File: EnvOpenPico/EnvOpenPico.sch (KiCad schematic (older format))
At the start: 55 parts, among them J2 SKRKAEE020, J3 2.54mm header 01x20, J4 2.54mm header 01x20, J5 Conn_01x03_Male, U1 TLV75533PDBVR, U3 RP2040, Y1 3225_4P

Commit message: some small adjustments
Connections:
- no-connect marks 5 -> 2
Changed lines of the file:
@@
 Wire Wire Line
 	14550 7600 14650 7600
-NoConn ~ 9050 6700
-NoConn ~ 9050 6800
-NoConn ~ 9050 7400
 NoConn ~ 1100 2000
 NoConn ~ 1100 1400

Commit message: added some notes and also various tweaks n what not.
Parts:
- FLASH1: value W25Q16 -> W25Q16FWUXIE
- RSW1: value Jumper_NO_Small -> SKRKAEE020
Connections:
- wire segments 219 -> 222
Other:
- note added: "JLCPCB Often has W25Q16FWUXIE in stock"
- note added: "Only fit cBP1 if you have selected an \nalternate voltage regulator\n\nTLV75533PDBVR does not require cBP1."
- note added: "not 22pf but pick to match crystal."
- note removed: "Only fit cBP1 if you have selected an \nalternate voltage regulator\n\nTLV75533PDBVR does not."
- moved on the sheet: PWRLED1, R12
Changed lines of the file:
@@
 P 3100 5250
 F 0 "FLASH1" H 3100 5250 50  0000 C CNN
-F 1 "W25Q16" H 3100 4750 50  0000 C CNN
+F 1 "W25Q16FWUXIE" H 3100 4750 50  0000 C CNN
 F 2 "Package_SON:SON-8-1EP_3x2mm_P0.5mm_EP1.4x1.6mm" H 3100 5250 50  0001 L BNN
 F 3 "" H 3100 5250 50  0001 L BNN
@@
 Wire Wire Line
 	3200 8400 3950 8400
-Text GLabel 6550 5800 0    50   Input ~ 0
+Text GLabel 6500 5800 0    50   Input ~ 0
 XIN
-Text GLabel 6550 6000 0    50   Input ~ 0
+Text GLabel 6500 6000 0    50   Input ~ 0
 XOUT
 Text GLabel 3950 8900 2    50   Input ~ 0
@@
 	4700 1850 4650 1850
 Text Notes 4450 2700 0    50   Italic 0
-Only fit cBP1 if you have selected an \nalternate voltage regulator\n\nTLV75533PDBVR does not.
+Only fit cBP1 if you have selected an \nalternate voltage regulator\n\nTLV75533PDBVR does not require cBP1.
 Text Notes 2200 6250 0    50   ~ 0
 GD25Q40CEIGR is NOT Compatible\nyou need GD25W16* needs to be a multiple of 8 atleast for circuitpython.
@@
 P 5800 6500
 F 0 "RSW1" H 5800 6600 50  0000 C CNN
-F 1 "Jumper_NO_Small" H 5950 6450 50  0000 C CNN
+F 1 "SKRKAEE020" H 5900 6400 50  0000 C CNN
 F 2 "Button_Switch_SMD:SW_Push_SPST_NO_Alps_SKRK" H 5800 6500 50  0001 C CNN
 F 3 "~" H 5800 6500 50  0001 C CNN
@@
 L Device:R R12
 U 1 1 614BB2FC
-P 14400 8000
-F 0 "R12" V 14193 8000 50  0000 C CNN
-F 1 "5.1K 0402 Resistor" V 14284 8000 50  0000 C CNN
-F 2 "Resistor_SMD:R_0402_1005Metric" V 14330 8000 50  0001 C CNN
-F 3 "" H 14400 8000 50  0001 C CNN
-F 4 " " H 14400 8000 50  0001 C CNN "LCSC"
-	1    14400 8000
+P 3100 2900
+F 0 "R12" V 2893 2900 50  0000 C CNN
+F 1 "5.1K 0402 Resistor" V 2984 2900 50  0000 C CNN
+F 2 "Resistor_SMD:R_0402_1005Metric" V 3030 2900 50  0001 C CNN
+F 3 "" H 3100 2900 50  0001 C CNN
+F 4 " " H 3100 2900 50  0001 C CNN "LCSC"
+	1    3100 2900
 	0    1    1    0
 $EndComp
@@
 L Device:LED PWRLED1
 U 1 1 614BBA4D
-P 14800 8000
-F 0 "PWRLED1" H 14750 7750 50  0000 C CNN
-F 1 "LED_0603" H 14600 7850 50  0000 C CNN
-F 2 "LED_SMD:LED_0603_1608Metric" H 14800 8000 50  0001 C CNN
-F 3 "" H 14800 8000 50  0001 C CNN
-F 4 " " H 14800 8000 50  0001 C CNN "LCSC"
-	1    14800 8000
+P 3500 2900
+F 0 "PWRLED1" H 3450 2650 50  0000 C CNN
+F 1 "LED_0603" H 3300 2750 50  0000 C CNN
+F 2 "LED_SMD:LED_0603_1608Metric" H 3500 2900 50  0001 C CNN
+F 3 "" H 3500 2900 50  0001 C CNN
+F 4 " " H 3500 2900 50  0001 C CNN "LCSC"
+	1    3500 2900
 	-1   0    0    1
 $EndComp
@@
 L power:GND #PWR0116
 U 1 1 614BBA57
-P 14950 8000
-F 0 "#PWR0116" H 14950 7750 50  0001 C CNN
-F 1 "GND" V 14955 7872 50  0000 R CNN
-F 2 "" H 14950 8000 50  0001 C CNN
-F 3 "" H 14950 8000 50  0001 C CNN
-	1    14950 8000
+P 3650 2900
+F 0 "#PWR0116" H 3650 2650 50  0001 C CNN
+F 1 "GND" V 3655 2772 50  0000 R CNN
+F 2 "" H 3650 2900 50  0001 C CNN
+F 3 "" H 3650 2900 50  0001 C CNN
+	1    3650 2900
 	0    -1   -1   0
 $EndComp
 Wire Wire Line
-	14550 8000 14650 8000
-Text Label 13850 8000 0    50   ~ 0
+	3250 2900 3350 2900
+Text Label 2550 2900 0    50   ~ 0
 VBUS
 Wire Wire Line
-	13850 8000 14250 8000
+	2550 2900 2950 2900
 Wire Wire Line
 	14250 7600 13850 7600
@@
 	11750 2900 11750 2850
 Connection ~ 11750 2850
+Wire Wire Line
+	3700 5550 3700 5350
+Connection ~ 3700 5550
+Text Notes 2200 6350 0    50   ~ 0
+JLCPCB Often has W25Q16FWUXIE in stock
+Text Notes 2850 8250 0    50   ~ 0
+not 22pf but pick to match crystal.
+Wire Wire Line
+	6500 5800 6550 5800
+Wire Wire Line
+	6550 6000 6500 6000
 $EndSCHEMATC

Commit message: corrected library symbol for reset button
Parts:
- RSW1: symbol Device:Jumper_NO_Small -> Switch:SW_Push
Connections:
- wire segments 222 -> 221
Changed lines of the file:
@@
 L power:GND #PWR0106
 U 1 1 6133A1A8
-P 5550 6550
-F 0 "#PWR0106" H 5550 6300 50  0001 C CNN
-F 1 "GND" H 5555 6377 50  0000 C CNN
-F 2 "" H 5550 6550 50  0001 C CNN
-F 3 "" H 5550 6550 50  0001 C CNN
-	1    5550 6550
+P 5400 6500
+F 0 "#PWR0106" H 5400 6250 50  0001 C CNN
+F 1 "GND" H 5405 6327 50  0000 C CNN
+F 2 "" H 5400 6500 50  0001 C CNN
+F 3 "" H 5400 6500 50  0001 C CNN
+	1    5400 6500
 	1    0    0    -1
 $EndComp
-Wire Wire Line
-	5550 6500 5550 6550
 $Comp
 L Regulator_Linear:AP131-15 U1
@@
 $EndComp
 $Comp
-L Device:Jumper_NO_Small RSW1
+L Switch:SW_Push RSW1
 U 1 1 6142C001
-P 5800 6500
-F 0 "RSW1" H 5800 6600 50  0000 C CNN
-F 1 "SKRKAEE020" H 5900 6400 50  0000 C CNN
-F 2 "Button_Switch_SMD:SW_Push_SPST_NO_Alps_SKRK" H 5800 6500 50  0001 C CNN
-F 3 "~" H 5800 6500 50  0001 C CNN
-	1    5800 6500
+P 5700 6500
+F 0 "RSW1" H 5700 6300 50  0000 C CNN
+F 1 "SKRKAEE020" H 5750 6400 50  0000 C CNN
+F 2 "Button_Switch_SMD:SW_Push_SPST_NO_Alps_SKRK" H 5700 6500 50  0001 C CNN
+F 3 "~" H 5700 6500 50  0001 C CNN
+	1    5700 6500
 	1    0    0    -1
 $EndComp
-Wire Wire Line
-	5550 6500 5700 6500
 Wire Wire Line
 	5900 6500 6550 6500
@@
 Wire Wire Line
 	6550 6000 6500 6000
+Wire Wire Line
+	5500 6500 5400 6500
 $EndSCHEMATC

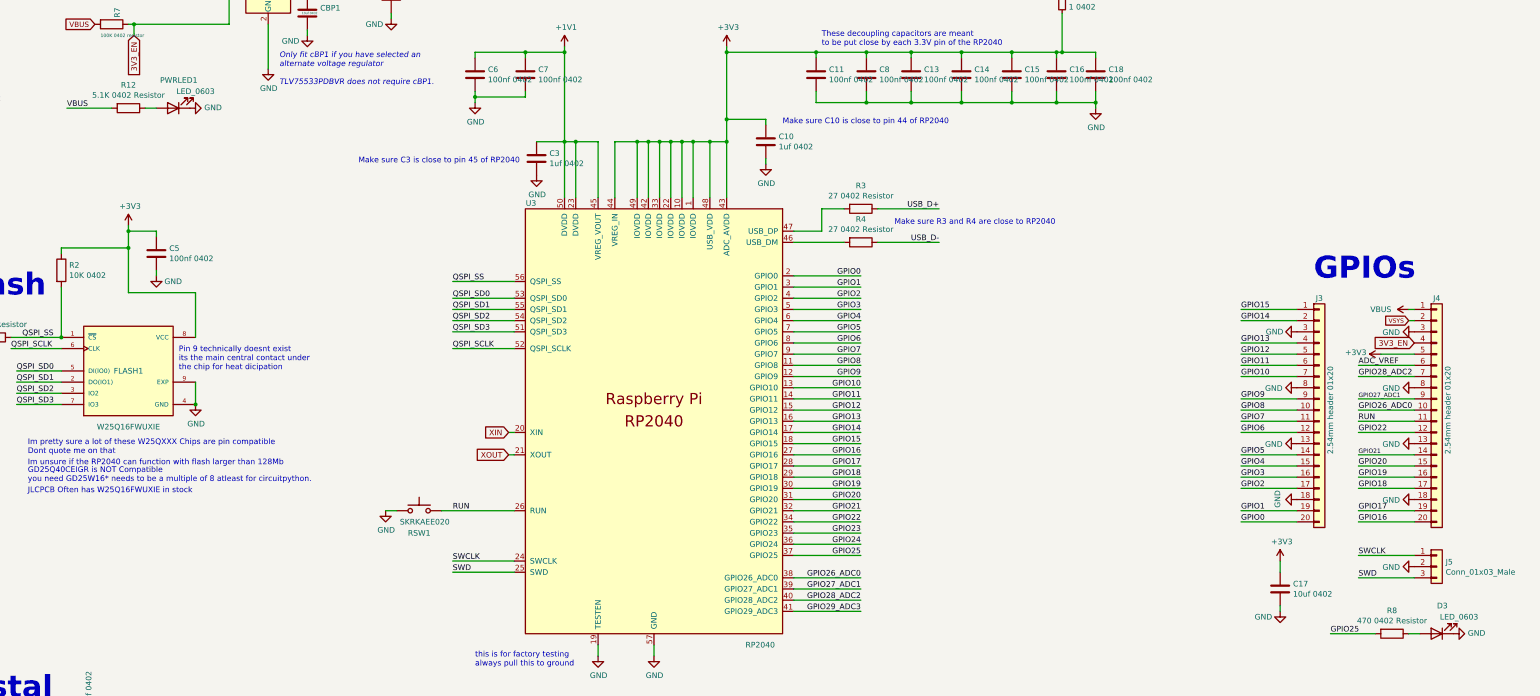
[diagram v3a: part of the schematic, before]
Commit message: updated gerbers and added generated gerber for version with BCPW Loco
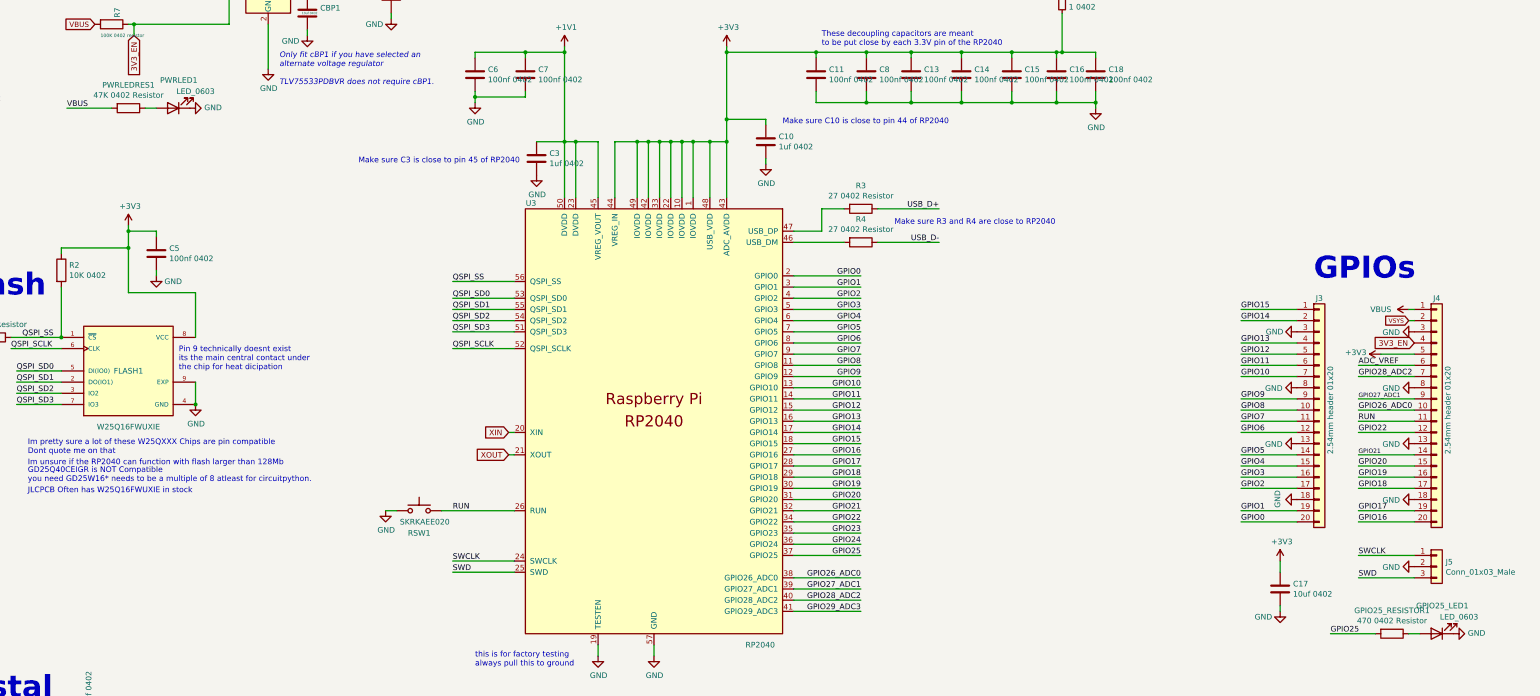
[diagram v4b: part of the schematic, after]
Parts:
- PWRLEDRES1: renamed from R12; value 5.1K 0402 Resistor -> 47K 0402 Resistor
- renumbered D3 to GPIO25_LED1, R8 to GPIO25_RESISTOR1
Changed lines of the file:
@@
 GPIO25
 $Comp
-L Device:R R8
+L Device:R GPIO25_RESISTOR1
 U 1 1 60CC69DF
 P 14400 7600
-F 0 "R8" V 14193 7600 50  0000 C CNN
+F 0 "GPIO25_RESISTOR1" V 14193 7600 50  0000 C CNN
 F 1 "470 0402 Resistor" V 14284 7600 50  0000 C CNN
 F 2 "Resistor_SMD:R_0402_1005Metric" V 14330 7600 50  0001 C CNN
@@
 $EndComp
 $Comp
-L Device:LED D3
+L Device:LED GPIO25_LED1
 U 1 1 60CC7B32
 P 14800 7600
-F 0 "D3" H 14750 7350 50  0000 C CNN
+F 0 "GPIO25_LED1" H 14750 7350 50  0000 C CNN
 F 1 "LED_0603" H 14600 7450 50  0000 C CNN
 F 2 "LED_SMD:LED_0603_1608Metric" H 14800 7600 50  0001 C CNN
@@
 	5900 6500 6550 6500
 $Comp
-L Device:R R12
+L Device:R PWRLEDRES1
 U 1 1 614BB2FC
 P 3100 2900
-F 0 "R12" V 2893 2900 50  0000 C CNN
-F 1 "5.1K 0402 Resistor" V 2984 2900 50  0000 C CNN
+F 0 "PWRLEDRES1" V 2893 2900 50  0000 C CNN
+F 1 "47K 0402 Resistor" V 2984 2900 50  0000 C CNN
 F 2 "Resistor_SMD:R_0402_1005Metric" V 3030 2900 50  0001 C CNN
 F 3 "" H 3100 2900 50  0001 C CNN

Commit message: swapped various parts to 0201 and added fuse between VSYS and linear reg
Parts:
- removed PWRLED1: LED_0603, LED_SMD:LED_0603_1608Metric, symbol Device:LED
- removed PWRLEDRES1: 47K 0402 Resistor, Resistor_SMD:R_0402_1005Metric, symbol Device:R
- removed TP3, TP4, TP5: TestPoint, TestPoint:TestPoint_Pad_D1.0mm, symbol Connector:TestPoint
- added F1: MF-FSMF035X-2, Fuse:Fuse_0603_1608Metric, symbol Device:Polyfuse_Small
- added GPIO24_LED1: LED_0402, LED_SMD:LED_0402_1005Metric, symbol Device:LED
- added GPIO24_RESISTOR1: 470 0402 Resistor, Resistor_SMD:R_0402_1005Metric, symbol Device:R
- added Q1: Si2329DS, Package_TO_SOT_SMD:SOT-23, symbol Transistor_FET:Si2319CDS
- C1: value 10uf 0603 6.3V -> 10uf 402; footprint Capacitor_SMD:C_0603_1608Metric -> Capacitor_SMD:C_0402_1005Metric
- C10, C3: value 1uf 0402 -> 1uf 0201; footprint Capacitor_SMD:C_0402_1005Metric -> Capacitor_SMD:C_0201_0603Metric
- C11, C13, C14, C15, C16, C18, C5, C6, C7, C8: value 100nf 0402 -> 100nf 0201; footprint Capacitor_SMD:C_0402_1005Metric -> Capacitor_SMD:C_0201_0603Metric
- GPIO25_LED1: value LED_0603 -> LED_0402; footprint LED_SMD:LED_0603_1608Metric -> LED_SMD:LED_0402_1005Metric
- R1, R11: value 1K 0402 Resistor -> 1K 0201; footprint Capacitor_SMD:C_0402_1005Metric -> Capacitor_SMD:C_0201_0603Metric
- R2: value 10K 0402 -> 10K 0201; footprint Capacitor_SMD:C_0402_1005Metric -> Capacitor_SMD:C_0201_0603Metric
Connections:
- net +3V3: now also Q1.2 (S)
- net GND: now also GPIO24_LED1.1 (K)
- net GPIO24: now also Q1.1 (G)
- net VSYS: now also F1.2; no longer C1.1, U1.1 (IN)
- new net: C1.1, F1.1, U1.1 (IN)
- new net: GPIO24_RESISTOR1.2, Q1.3 (D)
- new net: GPIO24_LED1.2 (A), GPIO24_RESISTOR1.1
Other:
- note added: "LEDs"
- moved on the sheet: C1, C17, GPIO25_LED1, GPIO25_RESISTOR1, J3, J4, J5

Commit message: corrected a placeholder reference I forgot to label as such, also added more comments in the schematic for the main design.
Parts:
- FLASH1: value W25Q16FWUXIE -> W25Q16JVUXIQ
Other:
- note added: "1K resistor to prevent overdriving of \nthe crystal as per the minimal design example"
- note added: "GD25Q40CEIGR is NOT Compatible\nyou need GD25W16* needs to be a multiple of 8 atleast for circuitpython.\n\n(Ive not confirmed if GD25W16 works I just \nHave some boards with GD25Q40CEIGR and they dont work)"
- note added: "Make sure the flash chip you\n have selected supports 3.3V\n power or adjust the design."
- note added: "Power LED is on by default but when\nGPIO24 is enabled it will be shut off"
- note added: "THIS FUSE MAY BE A TEMPOARY CHANGE"
- note added: "https://datasheets.raspberrypi.com/rp2040/hardware-design-with-rp2040.pdf\n\nOn page 13 you can learn more details of what flash is supported\n"
- note added: "suposedly the rp2040\nsupports SPI-2 flash\nbut I havent tried it.\n"
- note removed: "GD25Q40CEIGR is NOT Compatible\nyou need GD25W16* needs to be a multiple of 8 atleast for circuitpython."
- note removed: "JLCPCB Often has W25Q16FWUXIE in stock"
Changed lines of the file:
@@
 P 3100 5250
 F 0 "FLASH1" H 3100 5250 50  0000 C CNN
-F 1 "W25Q16FWUXIE" H 3100 4750 50  0000 C CNN
+F 1 "W25Q16JVUXIQ" H 3100 4750 50  0000 C CNN
 F 2 "Package_SON:SON-8-1EP_3x2mm_P0.5mm_EP1.4x1.6mm" H 3100 5250 50  0001 L BNN
 F 3 "" H 3100 5250 50  0001 L BNN
@@
 Text Notes 2600 9100 0    50   ~ 0
 RP2040 supports 1MHz to 15MHz
-Text Notes 2200 6000 0    50   ~ 0
+Text Notes 1950 6000 0    50   ~ 0
 Im pretty sure a lot of these W25QXXX Chips are pin compatible\nDont quote me on that
-Text Notes 2200 6100 0    50   ~ 0
+Text Notes 1950 6150 0    50   ~ 0
 Im unsure if the RP2040 can function with flash larger than 128Mb
 Text Notes 3550 5250 0    50   ~ 0
@@
 Text Notes 4450 2700 0    50   Italic 0
 Only fit cBP1 if you have selected an \nalternate voltage regulator\n\nTLV75533PDBVR does not require cBP1.
-Text Notes 2200 6250 0    50   ~ 0
-GD25Q40CEIGR is NOT Compatible\nyou need GD25W16* needs to be a multiple of 8 atleast for circuitpython.
+Text Notes 1950 6650 0    50   ~ 0
+GD25Q40CEIGR is NOT Compatible\nyou need GD25W16* needs to be a multiple of 8 atleast for circuitpython.\n\n(Ive not confirmed if GD25W16 works I just \nHave some boards with GD25Q40CEIGR and they dont work)
 $Comp
 L Device:R R11
@@
 	3700 5550 3700 5350
 Connection ~ 3700 5550
-Text Notes 2200 6350 0    50   ~ 0
-JLCPCB Often has W25Q16FWUXIE in stock
 Text Notes 2850 8250 0    50   ~ 0
 not 22pf but pick to match crystal.
@@
 U 1 1 61BEAA73
 P 14200 8950
-F 0 "Q1" H 14404 8996 50  0000 L CNN
-F 1 "Si2329DS" H 14404 8905 50  0000 L CNN
+F 0 "Q1" H 14350 8750 50  0000 L CNN
+F 1 "Si2329DS" H 14400 8850 50  0000 L CNN
 F 2 "Package_TO_SOT_SMD:SOT-23" H 14400 8875 50  0001 L CIN
 F 3 "http://www.vishay.com/docs/66709/si2319cd.pdf" H 14200 8950 50  0001 L CNN
@@
 Wire Wire Line
 	2850 1750 3500 1750
+Text Notes 1800 4000 0    50   ~ 0
+Make sure the flash chip you\n have selected supports 3.3V\n power or adjust the design.
+Text Notes 5750 4300 0    50   ~ 0
+suposedly the rp2040\nsupports SPI-2 flash\nbut I havent tried it.\n
+Text Notes 3800 8750 0    50   ~ 0
+1K resistor to prevent overdriving of \nthe crystal as per the minimal design example
+Text Notes 14500 8950 0    50   ~ 0
+Power LED is on by default but when\nGPIO24 is enabled it will be shut off
+Text Notes 1950 7000 0    50   ~ 0
+https://datasheets.raspberrypi.com/rp2040/hardware-design-with-rp2040.pdf\n\nOn page 13 you can learn more details of what flash is supported\n
+Text Notes 3600 1450 1    50   ~ 0
+THIS FUSE MAY BE A TEMPOARY CHANGE
 $EndSCHEMATC

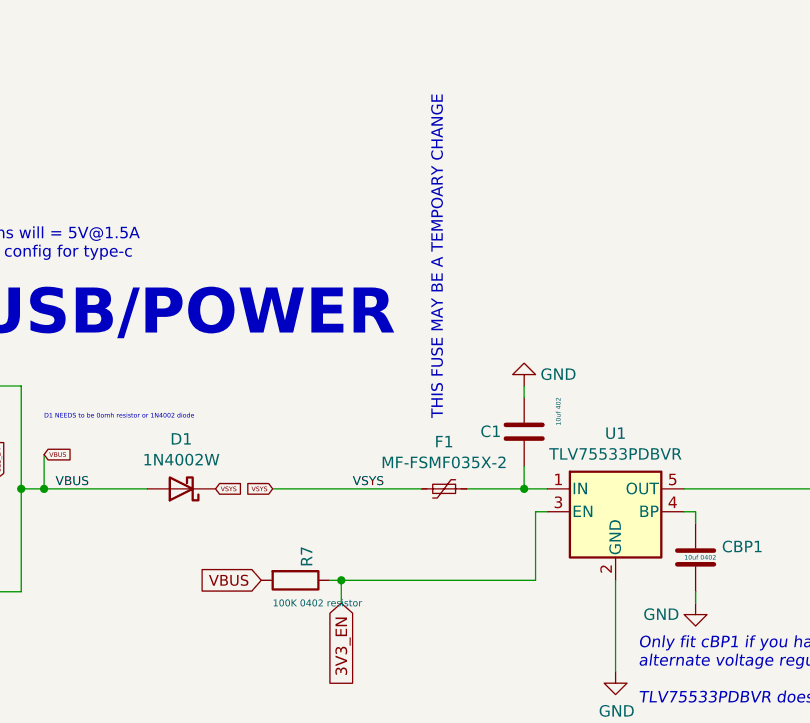
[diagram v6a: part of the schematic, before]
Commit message: removed Dip40 versions, changed fuse on main version to 805 size and added part number.
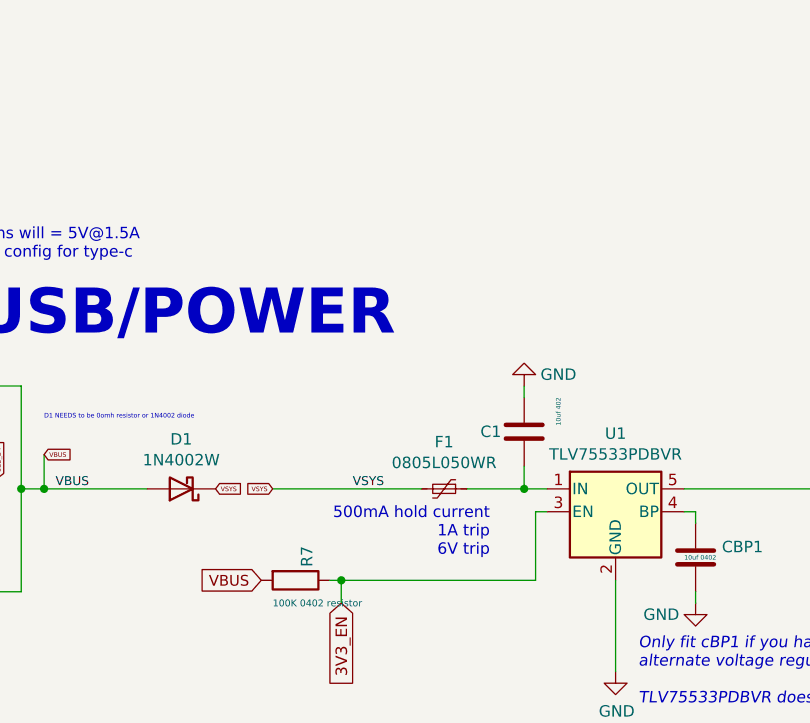
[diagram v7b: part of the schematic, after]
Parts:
- F1: value MF-FSMF035X-2 -> 0805L050WR; footprint Fuse:Fuse_0603_1608Metric -> Fuse:Fuse_0805_2012Metric
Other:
- note added: "500mA hold current\n1A trip\n6V trip"
- note removed: "THIS FUSE MAY BE A TEMPOARY CHANGE"
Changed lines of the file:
@@
 Wire Wire Line
 	4650 1750 5450 1750
-Wire Wire Line
-	4350 2150 4350 2550
 $Comp
 L Device:C CBP1
@@
 Wire Wire Line
 	4700 1850 4650 1850
-Text Notes 4450 2700 0    50   Italic 0
-Only fit cBP1 if you have selected an \nalternate voltage regulator\n\nTLV75533PDBVR does not require cBP1.
 Text Notes 1950 6650 0    50   ~ 0
 GD25Q40CEIGR is NOT Compatible\nyou need GD25W16* needs to be a multiple of 8 atleast for circuitpython.\n\n(Ive not confirmed if GD25W16 works I just \nHave some boards with GD25Q40CEIGR and they dont work)
@@
 P 3600 1750
 F 0 "F1" V 3395 1750 50  0000 C CNN
-F 1 "MF-FSMF035X-2" V 3486 1750 50  0000 C CNN
-F 2 "Fuse:Fuse_0603_1608Metric" H 3650 1550 50  0001 L CNN
+F 1 "0805L050WR" V 3486 1750 50  0000 C CNN
+F 2 "Fuse:Fuse_0805_2012Metric" H 3650 1550 50  0001 L CNN
 F 3 "~" H 3600 1750 50  0001 C CNN
 	1    3600 1750
@@
 Text Notes 1950 7000 0    50   ~ 0
 https://datasheets.raspberrypi.com/rp2040/hardware-design-with-rp2040.pdf\n\nOn page 13 you can learn more details of what flash is supported\n
-Text Notes 3600 1450 1    50   ~ 0
-THIS FUSE MAY BE A TEMPOARY CHANGE
+Text Notes 3800 2050 2    50   ~ 0
+500mA hold current\n1A trip\n6V trip
+Text Notes 4450 2700 0    50   Italic 0
+Only fit cBP1 if you have selected an \nalternate voltage regulator\n\nTLV75533PDBVR does not require cBP1.
+Wire Wire Line
+	4350 2150 4350 2550
 $EndSCHEMATC
